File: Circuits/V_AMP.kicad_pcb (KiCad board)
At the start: 2 copper layers, 103 x 154 mm, 138 parts, among them P1 INPUT, P2 GAIN_ADJ, P3 OUTPUT (0-5V), P4 POWER, U1 wOPA177, U2 LM393, U3 OPA177

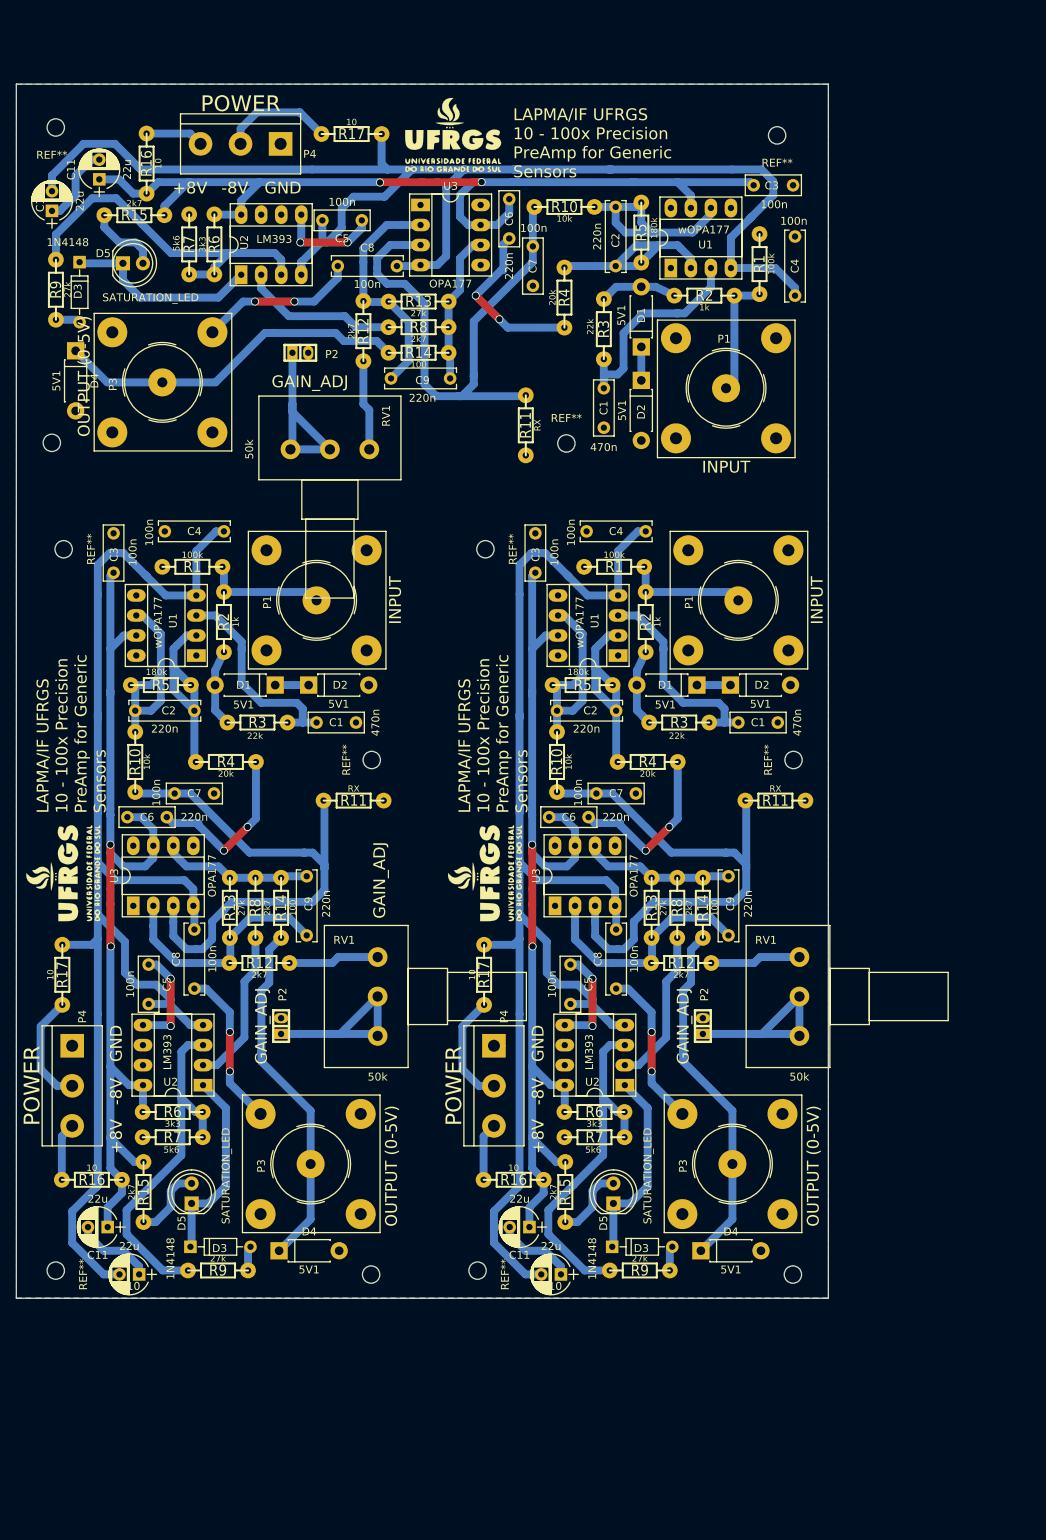
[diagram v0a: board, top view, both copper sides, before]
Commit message: Added full schematics and power supply
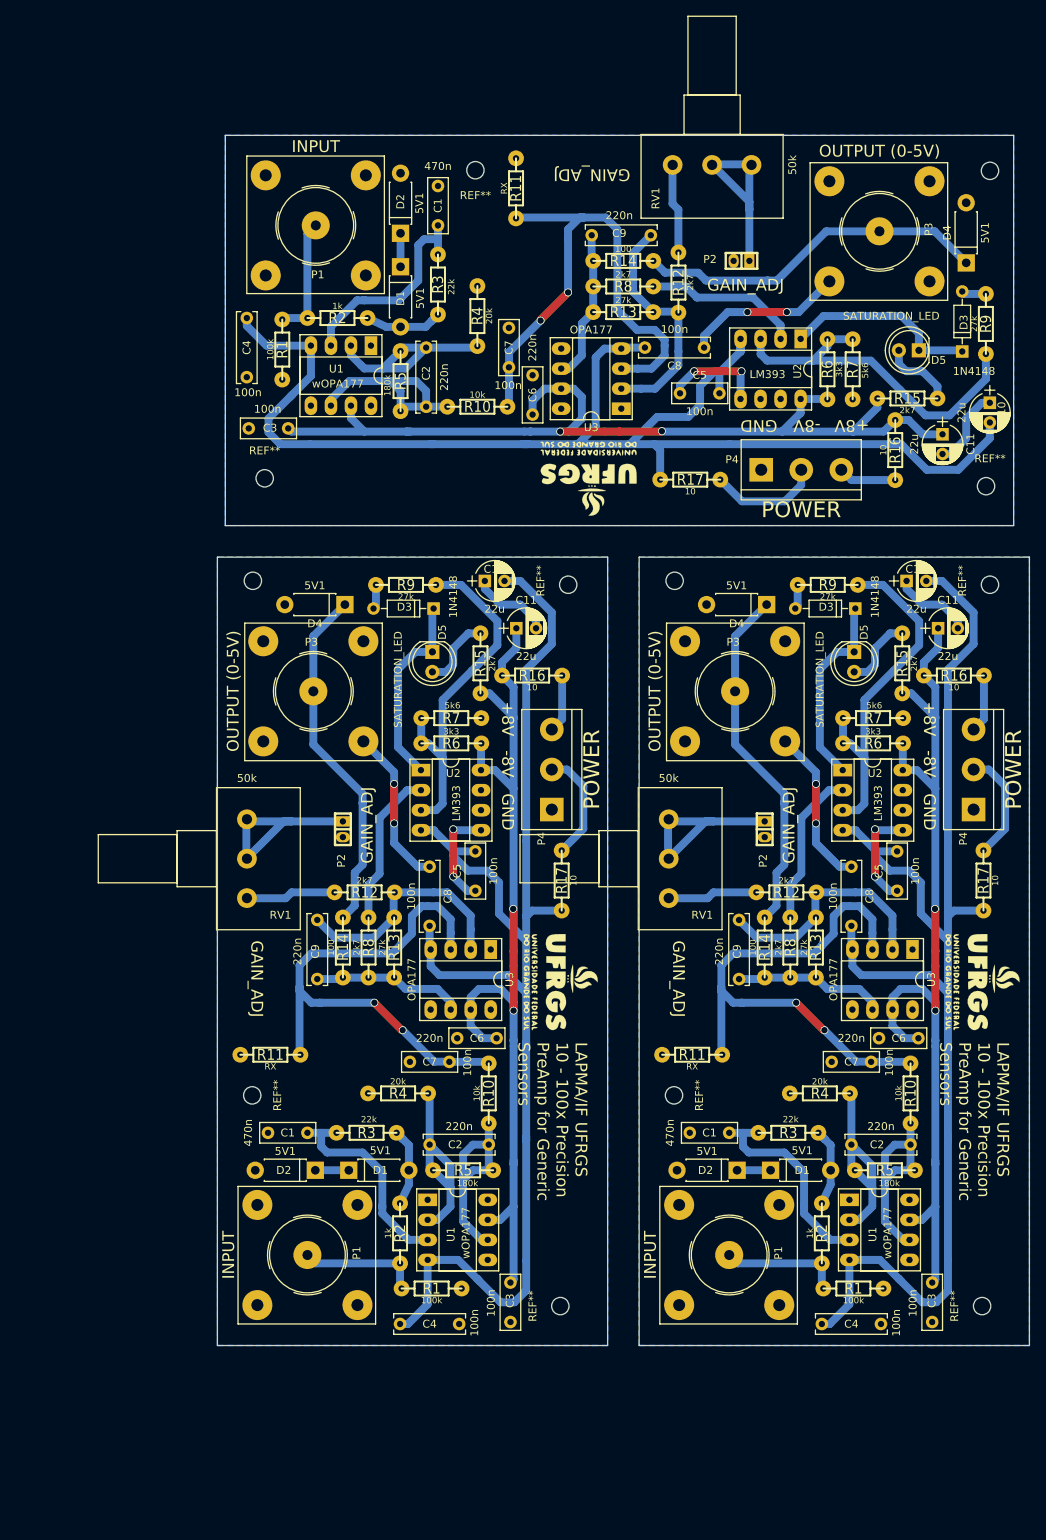
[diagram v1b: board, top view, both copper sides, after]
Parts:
- removed the C1 at (137.1, 100.0)
- removed the C1 at (83.6, 100.0)
- removed the C10 at (114.6, 170.0)
- removed the C10 at (61.1, 170.0)
- removed the C11 at (110.6, 164.0)
- removed the C11 at (57.1, 164.0)
- removed the C2 at (114.1, 98.5)
- removed the C2 at (60.6, 98.5)
- removed the C3 at (111.3, 76.0)
- removed the C3 at (57.8, 76.0)
- removed the C4 at (117.8, 75.7)
- removed the C4 at (64.3, 75.7)
- removed the C5 at (115.8, 130.7)
- removed the C5 at (62.3, 130.7)
- removed the C6 at (118.1, 112.0)
- removed the C6 at (64.6, 112.0)
- removed the C7 at (124.1, 109.0)
- removed the C7 at (70.6, 109.0)
- removed the C8 at (121.6, 133.7)
- removed the C8 at (68.1, 133.7)
- removed the C9 at (135.8, 127.0)
- removed the C9 at (82.3, 127.0)
- removed the D1 at (131.8, 95.2)
- removed the D1 at (78.3, 95.2)
- removed the D2 at (136.1, 95.2)
- removed the D2 at (82.6, 95.2)
- removed the D3 at (121.1, 166.5)
- removed the D3 at (67.6, 166.5)
- removed the D4 at (132.3, 167.0)
- removed the D4 at (78.8, 167.0)
- removed the D5 at (121.2, 161.0)
- removed the D5 at (67.7, 161.0)
- removed the G*** at (105.0, 119.0)
- removed the G*** at (51.5, 119.0)
- removed the P1 at (137.1, 84.5)
- removed the P1 at (83.6, 84.5)
- removed the P2 at (132.6, 138.5)
- removed the P2 at (79.1, 138.5)
- removed the P3 at (136.3, 156.0)
- removed the P3 at (82.8, 156.0)
- removed the P4 at (106.1, 141.0)
- removed the P4 at (52.6, 141.0)
- removed the R1 at (121.3, 80.2)
- removed the R1 at (67.8, 80.2)
- removed the R10 at (114.1, 105.0)
- removed the R10 at (60.6, 105.0)
- removed the R11 at (141.8, 109.9)
- removed the R11 at (88.3, 109.9)
- removed the R12 at (129.8, 130.5)
- removed the R12 at (76.3, 130.5)
- removed the R13 at (126.1, 123.5)
- removed the R13 at (72.6, 123.5)
- removed the R14 at (132.6, 123.5)
- removed the R14 at (79.1, 123.5)
- removed the R15 at (115.1, 159.5)
- removed the R15 at (61.6, 159.5)
- removed the R16 at (108.6, 158.0)
- removed the R16 at (55.1, 158.0)
- removed the R17 at (104.8, 132.0)
- removed the R17 at (51.3, 132.0)
- removed the R2 at (125.3, 87.2)
- removed the R2 at (71.8, 87.2)
- removed the R3 at (129.6, 100.0)
- removed the R3 at (76.1, 100.0)
- removed the R4 at (125.6, 105.0)
- removed the R4 at (72.1, 105.0)
- removed the R5 at (117.3, 95.2)
- removed the R5 at (63.8, 95.2)
- removed the R6 at (118.8, 149.4)
- removed the R6 at (65.3, 149.4)
- removed the R7 at (118.8, 152.6)
- removed the R7 at (65.3, 152.6)
- removed the R8 at (129.3, 123.5)
- removed the R8 at (75.8, 123.5)
- removed the R9 at (124.6, 169.5)
- removed the R9 at (71.1, 169.5)
- removed the REF** at (90.6, 104.7)
- removed the REF** at (90.5, 170.0)
- removed the REF** at (50.5, 169.5)
- removed the REF** at (104.0, 169.5)
- removed the REF** at (144.0, 170.0)
- removed the REF** at (144.1, 104.7)
- removed the REF** at (105.0, 78.0)
- removed the REF** at (51.5, 78.0)
- removed the RV1 at (144.8, 139.7)
- removed the RV1 at (91.3, 139.7)
- removed the U1 at (121.8, 91.5)
- removed the U1 at (68.3, 91.5)
- removed the U2 at (122.7, 146.0)
- removed the U2 at (69.2, 146.0)
- removed the U3 at (113.8, 123.2)
- removed the U3 at (60.3, 123.2)
- added C1: 470n, Capacitors_THT:C_Rect_L7.0mm_W2.5mm_P5.00mm, F.Cu at (99.0, 36.9)
- added C1: 470n, Capacitors_THT:C_Rect_L7.0mm_W2.5mm_P5.00mm, F.Cu at (135.9, 152.0)
- added C10: 22u, Capacitors_THT:CP_Radial_D5.0mm_P2.50mm, F.Cu at (169.0, 59.4)
- added C10: 22u, Capacitors_THT:CP_Radial_D5.0mm_P2.50mm, F.Cu at (158.4, 82.0)
- added C11: 22u, Capacitors_THT:CP_Radial_D5.0mm_P2.50mm, F.Cu at (163.0, 63.4)
- added C11: 22u, Capacitors_THT:CP_Radial_D5.0mm_P2.50mm, F.Cu at (162.4, 88.0)
- added C2: 220n, Capacitors_THT:C_Rect_L9.0mm_W2.5mm_P7.50mm_MKT, F.Cu at (97.5, 59.9)
- added C2: 220n, Capacitors_THT:C_Rect_L9.0mm_W2.5mm_P7.50mm_MKT, F.Cu at (158.9, 153.5)
- added C3: 100n, Capacitors_THT:C_Rect_L7.0mm_W2.5mm_P5.00mm, F.Cu at (75.0, 62.7)
- added C3: 100n, Capacitors_THT:C_Rect_L7.0mm_W2.5mm_P5.00mm, F.Cu at (161.7, 176.0)
- added C4: 100n, Capacitors_THT:C_Rect_L9.0mm_W2.5mm_P7.50mm_MKT, F.Cu at (74.7, 56.2)
- added C4: 100n, Capacitors_THT:C_Rect_L9.0mm_W2.5mm_P7.50mm_MKT, F.Cu at (155.2, 176.3)
- added C5: 100n, Capacitors_THT:C_Rect_L7.0mm_W2.5mm_P5.00mm, F.Cu at (129.7, 58.2)
- added C5: 100n, Capacitors_THT:C_Rect_L7.0mm_W2.5mm_P5.00mm, F.Cu at (157.2, 121.3)
- added C6: 100n, Capacitors_THT:C_Rect_L7.0mm_W2.5mm_P5.00mm, F.Cu at (111.0, 55.9)
- added C6: 100n, Capacitors_THT:C_Rect_L7.0mm_W2.5mm_P5.00mm, F.Cu at (154.9, 140.0)
- added C7: 220n, Capacitors_THT:C_Rect_L7.0mm_W2.5mm_P5.00mm, F.Cu at (108.0, 49.9)
- added C7: 220n, Capacitors_THT:C_Rect_L7.0mm_W2.5mm_P5.00mm, F.Cu at (148.9, 143.0)
- added C8: 100n, Capacitors_THT:C_Rect_L9.0mm_W2.5mm_P7.50mm_MKT, F.Cu at (132.7, 52.4)
- added C8: 100n, Capacitors_THT:C_Rect_L9.0mm_W2.5mm_P7.50mm_MKT, F.Cu at (151.4, 118.3)
- added C9: 220n, Capacitors_THT:C_Rect_L9.0mm_W2.5mm_P7.50mm_MKT, F.Cu at (126.0, 38.2)
- added C9: 220n, Capacitors_THT:C_Rect_L9.0mm_W2.5mm_P7.50mm_MKT, F.Cu at (137.2, 125.0)
- added D1: 5V1, Diodes_THT:D_DO-41_SOD81_P7.62mm_Horizontal, F.Cu at (94.2, 42.2)
- added D1: 5V1, Diodes_THT:D_DO-41_SOD81_P7.62mm_Horizontal, F.Cu at (141.2, 156.8)
- added D2: 5V1, Diodes_THT:D_DO-41_SOD81_P7.62mm_Horizontal, F.Cu at (94.2, 37.9)
- added D2: 5V1, Diodes_THT:D_DO-41_SOD81_P7.62mm_Horizontal, F.Cu at (136.9, 156.8)
- added D3: 1N4148, Diodes_THT:D_DO-35_SOD27_P7.62mm_Horizontal, F.Cu at (165.5, 52.9)
- added D3: 1N4148, Diodes_THT:D_DO-35_SOD27_P7.62mm_Horizontal, F.Cu at (151.9, 85.5)
- added D4: 5V1, Diodes_THT:D_DO-41_SOD81_P7.62mm_Horizontal, F.Cu at (166.0, 41.7)
- added D4: 5V1, Diodes_THT:D_DO-41_SOD81_P7.62mm_Horizontal, F.Cu at (140.7, 85.0)
- added D5: SATURATION_LED, LEDs:LED_D5.0mm, F.Cu at (160.0, 52.8)
- added D5: SATURATION_LED, LEDs:LED_D5.0mm, F.Cu at (151.8, 91.0)
- added G***: LOGO, Symbols:ufrgs, F.Cu at (118.0, 69.0)
- added G***: LOGO, Symbols:ufrgs, F.Cu at (168.0, 133.0)
- added P1: INPUT, Connectors:bnc-ci, F.Cu at (83.5, 36.9)
- added P1: INPUT, Connectors:bnc-ci, F.Cu at (135.9, 167.5)
- added P2: GAIN_ADJ, w_pin_strip:pin_strip_2mm_2, F.Cu at (137.5, 41.4)
- added P2: GAIN_ADJ, w_pin_strip:pin_strip_2mm_2, F.Cu at (140.4, 113.5)
- added P3: OUTPUT (0-5V), Connectors:bnc-ci, F.Cu at (155.0, 37.7)
- added P3: OUTPUT (0-5V), Connectors:bnc-ci, F.Cu at (136.7, 96.0)
- added P4: POWER, Connectors:bornier3, F.Cu at (140.0, 67.9)
- added P4: POWER, Connectors:bornier3, F.Cu at (166.9, 111.0)
- added R1: 100k, w_pth_resistors:RC03, F.Cu at (79.2, 52.7)
- added R1: 100k, w_pth_resistors:RC03, F.Cu at (151.7, 171.8)
- added R10: 10k, w_pth_resistors:RC03, F.Cu at (104.0, 59.9)
- added R10: 10k, w_pth_resistors:RC03, F.Cu at (158.9, 147.0)
- added R11: RX, w_pth_resistors:RC03, F.Cu at (108.9, 32.2)
- added R11: RX, w_pth_resistors:RC03, F.Cu at (131.2, 142.1)
- added R12: 2k7, w_pth_resistors:RC03, F.Cu at (129.5, 44.2)
- added R12: 2k7, w_pth_resistors:RC03, F.Cu at (143.2, 121.5)
- added R13: 27k, w_pth_resistors:RC03, F.Cu at (122.5, 47.9)
- added R13: 27k, w_pth_resistors:RC03, F.Cu at (146.9, 128.5)
- added R14: 100, w_pth_resistors:RC03, F.Cu at (122.5, 41.4)
- added R14: 100, w_pth_resistors:RC03, F.Cu at (140.4, 128.5)
- added R15: 2k7, w_pth_resistors:RC03, F.Cu at (158.5, 58.9)
- added R15: 2k7, w_pth_resistors:RC03, F.Cu at (157.9, 92.5)
- added R16: 10, w_pth_resistors:RC03, F.Cu at (157.0, 65.4)
- added R16: 10, w_pth_resistors:RC03, F.Cu at (164.4, 94.0)
- added R17: 10, w_pth_resistors:RC03, F.Cu at (131.0, 69.2)
- added R17: 10, w_pth_resistors:RC03, F.Cu at (168.2, 120.0)
- added R2: 1k, w_pth_resistors:RC03, F.Cu at (86.2, 48.7)
- added R2: 1k, w_pth_resistors:RC03, F.Cu at (147.7, 164.8)
- added R3: 22k, w_pth_resistors:RC03, F.Cu at (99.0, 44.4)
- added R3: 22k, w_pth_resistors:RC03, F.Cu at (143.4, 152.0)
- added R4: 20k, w_pth_resistors:RC03, F.Cu at (104.0, 48.4)
- added R4: 20k, w_pth_resistors:RC03, F.Cu at (147.4, 147.0)
- added R5: 180k, w_pth_resistors:RC03, F.Cu at (94.2, 56.7)
- added R5: 180k, w_pth_resistors:RC03, F.Cu at (155.7, 156.8)
- added R6: 3k3, w_pth_resistors:RC03, F.Cu at (148.4, 55.2)
- added R6: 3k3, w_pth_resistors:RC03, F.Cu at (154.2, 102.6)
- added R7: 5k6, w_pth_resistors:RC03, F.Cu at (151.6, 55.2)
- added R7: 5k6, w_pth_resistors:RC03, F.Cu at (154.2, 99.4)
- added R8: 2k7, w_pth_resistors:RC03, F.Cu at (122.5, 44.7)
- added R8: 2k7, w_pth_resistors:RC03, F.Cu at (143.7, 128.5)
- added R9: 27k, w_pth_resistors:RC03, F.Cu at (168.5, 49.4)
- added R9: 27k, w_pth_resistors:RC03, F.Cu at (148.4, 82.5)
- added REF**: MountingHole_2.2mm_M2, Mounting_Holes:MountingHole_2.2mm_M2, F.Cu at (77.0, 69.0)
- added REF**: MountingHole_2.2mm_M2, Mounting_Holes:MountingHole_2.2mm_M2, F.Cu at (103.7, 29.9)
- added REF**: MountingHole_2.2mm_M2, Mounting_Holes:MountingHole_2.2mm_M2, F.Cu at (169.0, 30.0)
- added REF**: MountingHole_2.2mm_M2, Mounting_Holes:MountingHole_2.2mm_M2, F.Cu at (168.5, 70.0)
- added REF**: MountingHole_2.2mm_M2, Mounting_Holes:MountingHole_2.2mm_M2, F.Cu at (168.0, 174.0)
- added REF**: MountingHole_2.2mm_M2, Mounting_Holes:MountingHole_2.2mm_M2, F.Cu at (128.9, 147.3)
- added REF**: MountingHole_2.2mm_M2, Mounting_Holes:MountingHole_2.2mm_M2, F.Cu at (129.0, 82.0)
- added REF**: MountingHole_2.2mm_M2, Mounting_Holes:MountingHole_2.2mm_M2, F.Cu at (169.0, 82.5)
- added RV1: 50k, Potentiometers:Potentiometer_Alps_RK163_Single_Vertical, F.Cu at (138.8, 29.2)
- added RV1: 50k, Potentiometers:Potentiometer_Alps_RK163_Single_Vertical, F.Cu at (128.2, 112.2)
- added U1: wOPA177, Housings_DIP:DIP-8_W7.62mm_Socket_LongPads, F.Cu at (90.5, 52.2)
- added U1: wOPA177, Housings_DIP:DIP-8_W7.62mm_Socket_LongPads, F.Cu at (151.2, 160.5)
- added U2: LM393, Housings_DIP:DIP-8_W7.62mm_Socket_LongPads, F.Cu at (145.0, 51.3)
- added U2: LM393, Housings_DIP:DIP-8_W7.62mm_Socket_LongPads, F.Cu at (150.3, 106.0)
- added U3: OPA177, Housings_DIP:DIP-8_W7.62mm_Socket_LongPads, F.Cu at (122.2, 60.2)
- added U3: OPA177, Housings_DIP:DIP-8_W7.62mm_Socket_LongPads, F.Cu at (159.2, 128.8)
- moved REF** 151.0 mm to (114.5, 174.0), turned to 270 degrees
- moved C3 148.6 mm to (108.2, 176.0), turned to 90 degrees
- moved C4 144.4 mm to (101.7, 176.3), turned to 180 degrees
- moved R1 136.4 mm to (98.2, 171.8), turned to 0 degrees
- moved R2 125.0 mm to (94.2, 164.8), turned to 270 degrees
- moved U1 122.1 mm to (97.7, 160.5), turned to 0 degrees
- moved P1 122.1 mm to (82.4, 167.5), turned to 270 degrees
- moved R5 121.1 mm to (102.2, 156.8), turned to 180 degrees
- moved C2 120.0 mm to (105.4, 153.5), turned to 180 degrees
- moved R10 112.8 mm to (105.4, 147.0), turned to 270 degrees
- moved D1 110.8 mm to (87.7, 156.8), turned to 0 degrees
- moved D2 108.4 mm to (83.4, 156.8), turned to 180 degrees
- moved G*** 108.3 mm to (114.5, 133.0), turned to 270 degrees
- moved R3 106.3 mm to (89.9, 152.0), turned to 0 degrees
- moved R4 103.1 mm to (93.9, 147.0), turned to 180 degrees
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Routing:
- net GND: track 200.2 -> 133.9 mm, vias 18 -> 12
- net Net-(C7-Pad2): vias 0 -> 6
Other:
- board size 103 x 154 mm -> 103 x 153.5 mm

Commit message: EDIT: Page SETUP
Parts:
- removed the C1 at (135.9, 152.0)
- removed the C1 at (82.4, 152.0)
- removed the C10 at (158.4, 82.0)
- removed the C10 at (104.9, 82.0)
- removed the C11 at (162.4, 88.0)
- removed the C11 at (108.9, 88.0)
- removed the C2 at (158.9, 153.5)
- removed the C2 at (105.4, 153.5)
- removed the C3 at (161.7, 176.0)
- removed the C3 at (108.2, 176.0)
- removed the C4 at (155.2, 176.3)
- removed the C4 at (101.7, 176.3)
- removed the C5 at (157.2, 121.3)
- removed the C5 at (103.7, 121.3)
- removed the C6 at (154.9, 140.0)
- removed the C6 at (101.4, 140.0)
- removed the C7 at (148.9, 143.0)
- removed the C7 at (95.4, 143.0)
- removed the C8 at (151.4, 118.3)
- removed the C8 at (97.9, 118.3)
- removed the C9 at (137.2, 125.0)
- removed the C9 at (83.7, 125.0)
- removed the D1 at (141.2, 156.8)
- removed the D1 at (87.7, 156.8)
- removed the D2 at (136.9, 156.8)
- removed the D2 at (83.4, 156.8)
- removed the D3 at (151.9, 85.5)
- removed the D3 at (98.4, 85.5)
- removed the D4 at (140.7, 85.0)
- removed the D4 at (87.2, 85.0)
- removed the D5 at (151.8, 91.0)
- removed the D5 at (98.3, 91.0)
- removed the G*** at (168.0, 133.0)
- removed the G*** at (114.5, 133.0)
- removed the P1 at (135.9, 167.5)
- removed the P1 at (82.4, 167.5)
- removed the P2 at (140.4, 113.5)
- removed the P2 at (86.9, 113.5)
- removed the P3 at (136.7, 96.0)
- removed the P3 at (83.2, 96.0)
- removed the P4 at (166.9, 111.0)
- removed the P4 at (113.4, 111.0)
- removed the R1 at (151.7, 171.8)
- removed the R1 at (98.2, 171.8)
- removed the R10 at (158.9, 147.0)
- removed the R10 at (105.4, 147.0)
- removed the R11 at (131.2, 142.1)
- removed the R11 at (77.7, 142.1)
- removed the R12 at (143.2, 121.5)
- removed the R12 at (89.7, 121.5)
- removed the R13 at (146.9, 128.5)
- removed the R13 at (93.4, 128.5)
- removed the R14 at (140.4, 128.5)
- removed the R14 at (86.9, 128.5)
- removed the R15 at (157.9, 92.5)
- removed the R15 at (104.4, 92.5)
- removed the R16 at (164.4, 94.0)
- removed the R16 at (110.9, 94.0)
- removed the R17 at (168.2, 120.0)
- removed the R17 at (114.7, 120.0)
- removed the R2 at (147.7, 164.8)
- removed the R2 at (94.2, 164.8)
- removed the R3 at (143.4, 152.0)
- removed the R3 at (89.9, 152.0)
- removed the R4 at (147.4, 147.0)
- removed the R4 at (93.9, 147.0)
- removed the R5 at (155.7, 156.8)
- removed the R5 at (102.2, 156.8)
- removed the R6 at (154.2, 102.6)
- removed the R6 at (100.7, 102.6)
- removed the R7 at (154.2, 99.4)
- removed the R7 at (100.7, 99.4)
- removed the R8 at (143.7, 128.5)
- removed the R8 at (90.2, 128.5)
- removed the R9 at (148.4, 82.5)
- removed the R9 at (94.9, 82.5)
- removed the REF** at (75.5, 82.0)
- removed the REF** at (75.4, 147.3)
- removed the REF** at (114.5, 174.0)
- removed the REF** at (168.0, 174.0)
- removed the REF** at (128.9, 147.3)
- removed the REF** at (129.0, 82.0)
- removed the REF** at (169.0, 82.5)
- removed the REF** at (115.5, 82.5)
- removed the RV1 at (128.2, 112.2)
- removed the RV1 at (74.8, 112.2)
- removed the U1 at (151.2, 160.5)
- removed the U1 at (97.7, 160.5)
- removed the U2 at (150.3, 106.0)
- removed the U2 at (96.8, 106.0)
- removed the U3 at (159.2, 128.8)
- removed the U3 at (105.7, 128.8)
- added C1: 470n, Capacitors_THT:C_Rect_L7.0mm_W2.5mm_P5.00mm, F.Cu at (142.3, 59.7)
- added C1: 470n, Capacitors_THT:C_Rect_L7.0mm_W2.5mm_P5.00mm, F.Cu at (88.3, 59.7)
- added C10: 22u, Capacitors_THT:CP_Radial_D5.0mm_P2.50mm, F.Cu at (119.8, 129.7)
- added C10: 22u, Capacitors_THT:CP_Radial_D5.0mm_P2.50mm, F.Cu at (65.8, 129.7)
- added C11: 22u, Capacitors_THT:CP_Radial_D5.0mm_P2.50mm, F.Cu at (115.8, 123.7)
- added C11: 22u, Capacitors_THT:CP_Radial_D5.0mm_P2.50mm, F.Cu at (61.8, 123.7)
- added C2: 220n, Capacitors_THT:C_Rect_L9.0mm_W2.5mm_P7.50mm_MKT, F.Cu at (119.3, 58.2)
- added C2: 220n, Capacitors_THT:C_Rect_L9.0mm_W2.5mm_P7.50mm_MKT, F.Cu at (65.3, 58.2)
- added C3: 100n, Capacitors_THT:C_Rect_L7.0mm_W2.5mm_P5.00mm, F.Cu at (116.6, 35.7)
- added C3: 100n, Capacitors_THT:C_Rect_L7.0mm_W2.5mm_P5.00mm, F.Cu at (62.6, 35.7)
- added C4: 100n, Capacitors_THT:C_Rect_L9.0mm_W2.5mm_P7.50mm_MKT, F.Cu at (123.1, 35.5)
- added C4: 100n, Capacitors_THT:C_Rect_L9.0mm_W2.5mm_P7.50mm_MKT, F.Cu at (69.1, 35.5)
- added C5: 100n, Capacitors_THT:C_Rect_L7.0mm_W2.5mm_P5.00mm, F.Cu at (121.0, 90.4)
- added C5: 100n, Capacitors_THT:C_Rect_L7.0mm_W2.5mm_P5.00mm, F.Cu at (67.0, 90.4)
- added C6: 100n, Capacitors_THT:C_Rect_L7.0mm_W2.5mm_P5.00mm, F.Cu at (123.3, 71.7)
- added C6: 100n, Capacitors_THT:C_Rect_L7.0mm_W2.5mm_P5.00mm, F.Cu at (69.3, 71.7)
- added C7: 220n, Capacitors_THT:C_Rect_L7.0mm_W2.5mm_P5.00mm, F.Cu at (129.3, 68.7)
- added C7: 220n, Capacitors_THT:C_Rect_L7.0mm_W2.5mm_P5.00mm, F.Cu at (75.3, 68.7)
- added C8: 100n, Capacitors_THT:C_Rect_L9.0mm_W2.5mm_P7.50mm_MKT, F.Cu at (126.8, 93.5)
- added C8: 100n, Capacitors_THT:C_Rect_L9.0mm_W2.5mm_P7.50mm_MKT, F.Cu at (72.8, 93.5)
- added C9: 220n, Capacitors_THT:C_Rect_L9.0mm_W2.5mm_P7.50mm_MKT, F.Cu at (141.1, 86.7)
- added C9: 220n, Capacitors_THT:C_Rect_L9.0mm_W2.5mm_P7.50mm_MKT, F.Cu at (87.1, 86.7)
- added D1: 5V1, Diodes_THT:D_DO-41_SOD81_P7.62mm_Horizontal, F.Cu at (137.1, 55.0)
- added D1: 5V1, Diodes_THT:D_DO-41_SOD81_P7.62mm_Horizontal, F.Cu at (83.1, 55.0)
- added D2: 5V1, Diodes_THT:D_DO-41_SOD81_P7.62mm_Horizontal, F.Cu at (141.3, 55.0)
- added D2: 5V1, Diodes_THT:D_DO-41_SOD81_P7.62mm_Horizontal, F.Cu at (87.3, 55.0)
- added D3: 1N4148, Diodes_THT:D_DO-35_SOD27_P7.62mm_Horizontal, F.Cu at (126.3, 126.2)
- added D3: 1N4148, Diodes_THT:D_DO-35_SOD27_P7.62mm_Horizontal, F.Cu at (72.3, 126.2)
- added D4: 5V1, Diodes_THT:D_DO-41_SOD81_P7.62mm_Horizontal, F.Cu at (137.6, 126.7)
- added D4: 5V1, Diodes_THT:D_DO-41_SOD81_P7.62mm_Horizontal, F.Cu at (83.6, 126.7)
- added D5: SATURATION_LED, LEDs:LED_D5.0mm, F.Cu at (126.5, 120.7)
- added D5: SATURATION_LED, LEDs:LED_D5.0mm, F.Cu at (72.5, 120.7)
- added G***: LOGO, Symbols:ufrgs, F.Cu at (110.2, 78.8)
- added G***: LOGO, Symbols:ufrgs, F.Cu at (56.2, 78.8)
- added P1: INPUT, Connectors:bnc-ci, F.Cu at (142.3, 44.2)
- added P1: INPUT, Connectors:bnc-ci, F.Cu at (88.3, 44.2)
- added P2: GAIN_ADJ, w_pin_strip:pin_strip_2mm_2, F.Cu at (137.8, 98.2)
- added P2: GAIN_ADJ, w_pin_strip:pin_strip_2mm_2, F.Cu at (83.8, 98.2)
- added P3: OUTPUT (0-5V), Connectors:bnc-ci, F.Cu at (141.6, 115.7)
- added P3: OUTPUT (0-5V), Connectors:bnc-ci, F.Cu at (87.6, 115.7)
- added P4: POWER, Connectors:bornier3, F.Cu at (111.3, 100.7)
- added P4: POWER, Connectors:bornier3, F.Cu at (57.3, 100.7)
- added R1: 100k, w_pth_resistors:RC03, F.Cu at (126.6, 40.0)
- added R1: 100k, w_pth_resistors:RC03, F.Cu at (72.6, 40.0)
- added R10: 10k, w_pth_resistors:RC03, F.Cu at (119.3, 64.7)
- added R10: 10k, w_pth_resistors:RC03, F.Cu at (65.3, 64.7)
- added R11: RX, w_pth_resistors:RC03, F.Cu at (147.0, 69.6)
- added R11: RX, w_pth_resistors:RC03, F.Cu at (93.0, 69.6)
- added R12: 2k7, w_pth_resistors:RC03, F.Cu at (135.1, 90.2)
- added R12: 2k7, w_pth_resistors:RC03, F.Cu at (81.1, 90.2)
- added R13: 27k, w_pth_resistors:RC03, F.Cu at (131.3, 83.2)
- added R13: 27k, w_pth_resistors:RC03, F.Cu at (77.3, 83.2)
- added R14: 100, w_pth_resistors:RC03, F.Cu at (137.8, 83.2)
- added R14: 100, w_pth_resistors:RC03, F.Cu at (83.8, 83.2)
- added R15: 2k7, w_pth_resistors:RC03, F.Cu at (120.4, 119.3)
- added R15: 2k7, w_pth_resistors:RC03, F.Cu at (66.4, 119.3)
- added R16: 10, w_pth_resistors:RC03, F.Cu at (113.8, 117.7)
- added R16: 10, w_pth_resistors:RC03, F.Cu at (59.8, 117.7)
- added R17: 10, w_pth_resistors:RC03, F.Cu at (110.1, 91.7)
- added R17: 10, w_pth_resistors:RC03, F.Cu at (56.1, 91.7)
- added R2: 1k, w_pth_resistors:RC03, F.Cu at (130.6, 47.0)
- added R2: 1k, w_pth_resistors:RC03, F.Cu at (76.6, 47.0)
- added R3: 22k, w_pth_resistors:RC03, F.Cu at (134.8, 59.7)
- added R3: 22k, w_pth_resistors:RC03, F.Cu at (80.8, 59.7)
- added R4: 20k, w_pth_resistors:RC03, F.Cu at (130.8, 64.7)
- added R4: 20k, w_pth_resistors:RC03, F.Cu at (76.8, 64.7)
- added R5: 180k, w_pth_resistors:RC03, F.Cu at (122.6, 55.0)
- added R5: 180k, w_pth_resistors:RC03, F.Cu at (68.6, 55.0)
- added R6: 3k3, w_pth_resistors:RC03, F.Cu at (124.1, 109.1)
- added R6: 3k3, w_pth_resistors:RC03, F.Cu at (70.1, 109.1)
- added R7: 5k6, w_pth_resistors:RC03, F.Cu at (124.1, 112.3)
- added R7: 5k6, w_pth_resistors:RC03, F.Cu at (70.1, 112.3)
- added R8: 2k7, w_pth_resistors:RC03, F.Cu at (134.6, 83.2)
- added R8: 2k7, w_pth_resistors:RC03, F.Cu at (80.6, 83.2)
- added R9: 27k, w_pth_resistors:RC03, F.Cu at (129.8, 129.2)
- added R9: 27k, w_pth_resistors:RC03, F.Cu at (75.8, 129.2)
- added REF**: MountingHole_2.2mm_M2, Mounting_Holes:MountingHole_2.2mm_M2, F.Cu at (110.2, 37.8)
- added REF**: MountingHole_2.2mm_M2, Mounting_Holes:MountingHole_2.2mm_M2, F.Cu at (149.3, 64.5)
- added REF**: MountingHole_2.2mm_M2, Mounting_Holes:MountingHole_2.2mm_M2, F.Cu at (149.2, 129.8)
- added REF**: MountingHole_2.2mm_M2, Mounting_Holes:MountingHole_2.2mm_M2, F.Cu at (109.2, 129.2)
- added REF**: MountingHole_2.2mm_M2, Mounting_Holes:MountingHole_2.2mm_M2, F.Cu at (55.2, 129.2)
- added REF**: MountingHole_2.2mm_M2, Mounting_Holes:MountingHole_2.2mm_M2, F.Cu at (95.2, 129.8)
- added REF**: MountingHole_2.2mm_M2, Mounting_Holes:MountingHole_2.2mm_M2, F.Cu at (95.3, 64.5)
- added REF**: MountingHole_2.2mm_M2, Mounting_Holes:MountingHole_2.2mm_M2, F.Cu at (56.2, 37.8)
- added RV1: 50k, Potentiometers:Potentiometer_Alps_RK163_Single_Vertical, F.Cu at (104.8, 112.8)
- added RV1: 50k, Potentiometers:Potentiometer_Alps_RK163_Single_Vertical, F.Cu at (78.8, 101.2)
- added U1: OPA277, Housings_DIP:DIP-8_W7.62mm_Socket_LongPads, F.Cu at (127.1, 51.2)
- added U1: OPA277, Housings_DIP:DIP-8_W7.62mm_Socket_LongPads, F.Cu at (73.1, 51.2)
- added U2: LM393, Housings_DIP:DIP-8_W7.62mm_Socket_LongPads, F.Cu at (127.9, 105.7)
- added U2: LM393, Housings_DIP:DIP-8_W7.62mm_Socket_LongPads, F.Cu at (73.9, 105.7)
- added U3: OPA277, Housings_DIP:DIP-8_W7.62mm_Socket_LongPads, F.Cu at (119.1, 83.0)
- added U3: OPA277, Housings_DIP:DIP-8_W7.62mm_Socket_LongPads, F.Cu at (65.1, 83.0)
- U1: value wOPA177 -> OPA277
- U3: value OPA177 -> OPA277
- moved REF** 190.0 mm to (55.0, 182.0), turned to 0 degrees
- moved D4 168.0 mm to (58.0, 170.3), turned to 270 degrees
- moved RV1 162.6 mm to (85.2, 182.8), turned to 270 degrees
- moved P3 161.4 mm to (69.0, 174.3), turned to 90 degrees
- moved R9 159.9 mm to (55.5, 162.6), turned to 90 degrees
- moved REF** 153.1 mm to (120.3, 182.1), turned to 0 degrees
- moved D3 150.7 mm to (58.5, 159.1), turned to 270 degrees
- moved P1 149.5 mm to (140.5, 175.1), turned to 0 degrees
- moved R11 147.7 mm to (115.1, 179.8), turned to 90 degrees
- moved C10 147.2 mm to (55.0, 152.6), turned to 90 degrees
- moved D5 143.3 mm to (64.0, 159.2), turned to 0 degrees
- moved D2 140.7 mm to (129.8, 174.1), turned to 270 degrees
- moved C1 140.6 mm to (125.0, 175.1), turned to 270 degrees
- moved P2 138.8 mm to (86.5, 170.6), turned to 0 degrees
- moved C9 138.5 mm to (98.0, 173.8), turned to 0 degrees
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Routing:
- net Net-(P4-Pad3): track 23.5 -> 16.1 mm
- net Net-(P2-Pad1): track 76.3 -> 83.7 mm
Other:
- board size 103 x 153.5 mm -> 103.5 x 153.8 mm
